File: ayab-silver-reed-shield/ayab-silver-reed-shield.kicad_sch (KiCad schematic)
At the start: 16 parts, among them J1 Power, J2 Digital/PWM, J3 Analog, J4 Digital/PWM, J5 DIN-7, J6 Barrel_Jack, K1 Relay_SPDT, Q1 2N2222A-TO92

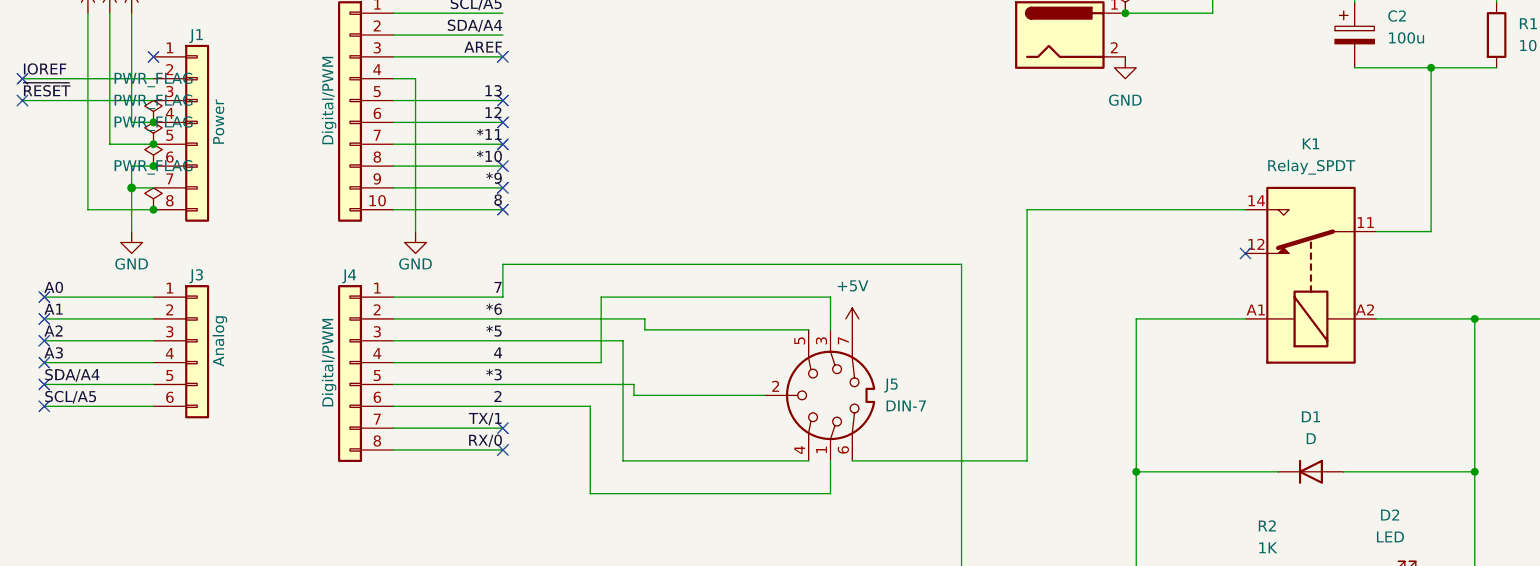
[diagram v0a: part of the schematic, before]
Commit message: Add footprints
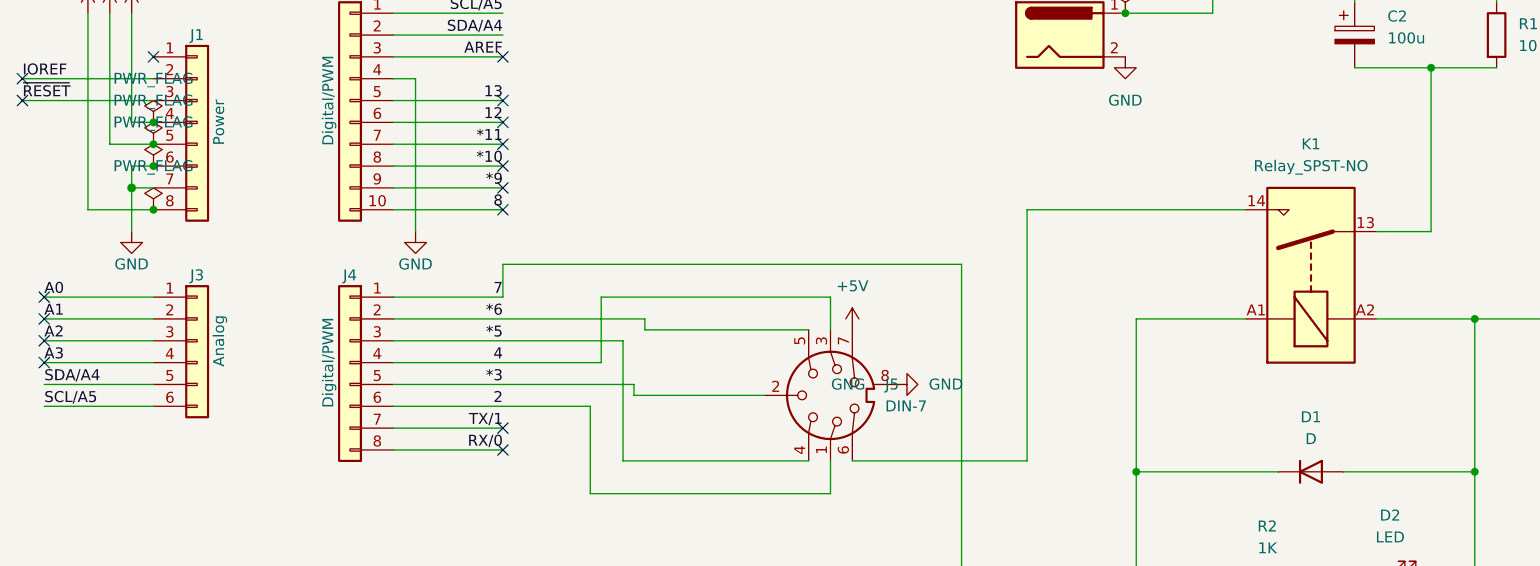
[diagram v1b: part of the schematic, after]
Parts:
- removed K1: Relay_SPDT, symbol Relay:Relay_SPDT
- added K1: Relay_SPST-NO, Locals:RELAY_G6DN-1A_OMR, symbol Relay:Relay_SPST-NO
- C2: footprint (none) -> Capacitor_THT:CP_Radial_D6.3mm_P2.50mm
- D1: footprint (none) -> Diode_THT:D_T-1_P5.08mm_Horizontal
- D2, D3: footprint (none) -> LED_THT:LED_D5.0mm
- J5: footprint (none) -> Connector_DIN:DIN-704-M10
- J6: footprint (none) -> Connector_BarrelJack:BarrelJack_Horizontal
- R1: footprint (none) -> Resistor_THT:R_Axial_Power_L20.0mm_W6.4mm_P25.40mm
- R2, R3: footprint (none) -> Resistor_THT:R_Axial_DIN0207_L6.3mm_D2.5mm_P7.62mm_Horizontal
- R4: footprint (none) -> Resistor_THT:R_Axial_DIN0207_L6.3mm_D2.5mm_P10.16mm_Horizontal
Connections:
- net +5V: now also K1.A1
- net GND: now also J5.8 (GNG)
- net at D1.2 (A), D2.1 (K), Q1.3 (C): now also K1.A2
- net at C2.2, R1.2: now also K1.13
- net at J5.6: now also K1.14
- no-connect marks 19 -> 16
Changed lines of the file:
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@@
 	)
 	(no_connect
-		(at 161.29 54.61)
-	)
-	(no_connect
 		(at 74.93 39.37)
 	)
@@
 	)
 	(no_connect
-		(at 21.59 69.85)
-	)
-	(no_connect
 		(at 21.59 64.77)
 	)
 	(no_connect
-		(at 21.59 72.39)
-	)
-	(no_connect
 		(at 21.59 59.69)
 	)
@@
 	)
 	(symbol
+		(lib_id "power:GND")
+		(at 120.65 69.85 90)
+		(unit 1)
+		(exclude_from_sim no)
+		(in_bom yes)
+		(on_board yes)
+		(dnp no)
+		(fields_autoplaced yes)
+		(property "Reference" "#PWR06"
+			(at 127 69.85 0)
+			(effects
+				(font
+					(size 1.27 1.27)
+				)
+				(hide yes)
+			)
+		)
+		(property "Value" "GND"
+			(at 124.46 69.8499 90)
+			(effects
+				(font
+					(size 1.27 1.27)
+				)
+				(justify right)
+			)
+		)
+		(property "Footprint" ""
+			(at 120.65 69.85 0)
+			(effects
+				(font
+					(size 1.27 1.27)
+				)
+				(hide yes)
+			)
+		)
+		(property "Datasheet" ""
+			(at 120.65 69.85 0)
+			(effects
+				(font
+					(size 1.27 1.27)
+				)
+				(hide yes)
+			)
+		)
+		(property "Description" "Power symbol creates a global label with name \"GND\" , ground"
+			(at 120.65 69.85 0)
+			(effects
+				(font
+					(size 1.27 1.27)
+				)
+				(hide yes)
+			)
+		)
+		(pin "1"
+		)
+		(instances
+			(project ""
+				(path "/e63e39d7-6ac0-4ffd-8aa3-1841a4541b55"
+					(reference "#PWR06")
+					(unit 1)
+				)
+			)
+		)
+	)
+	(symbol
 		(lib_id "Device:R")
 		(at 163.83 92.71 270)
@@
 			)
 		)
-		(property "Footprint" ""
+		(property "Footprint" "Resistor_THT:R_Axial_DIN0207_L6.3mm_D2.5mm_P7.62mm_Horizontal"
 			(at 163.83 90.932 90)
 			(effects
@@
 			)
 		)
-		(property "Footprint" ""
+		(property "Footprint" "Connector_BarrelJack:BarrelJack_Horizontal"
 			(at 140.97 30.226 0)
 			(effects
@@
 			)
 		)
-		(property "Footprint" ""
+		(property "Footprint" "Diode_THT:D_T-1_P5.08mm_Horizontal"
 			(at 168.91 80.01 0)
 			(effects
@@
 			)
 		)
-		(property "Footprint" ""
+		(property "Footprint" "Resistor_THT:R_Axial_DIN0207_L6.3mm_D2.5mm_P7.62mm_Horizontal"
 			(at 202.692 82.55 90)
 			(effects
@@
 			)
 		)
-		(property "Footprint" ""
+		(property "Footprint" "Resistor_THT:R_Axial_DIN0207_L6.3mm_D2.5mm_P10.16mm_Horizontal"
 			(at 163.83 101.092 90)
 			(effects
@@
 			)
 		)
-		(property "Footprint" ""
+		(property "Footprint" "LED_THT:LED_D5.0mm"
 			(at 176.53 102.87 0)
 			(effects
@@
 			)
 		)
-		(property "Footprint" ""
+		(property "Footprint" "Capacitor_THT:CP_Radial_D6.3mm_P2.50mm"
 			(at 174.9552 33.02 0)
 			(effects
@@
 			)
 		)
-		(property "Footprint" ""
+		(property "Footprint" "Resistor_THT:R_Axial_Power_L20.0mm_W6.4mm_P25.40mm"
 			(at 188.722 29.21 90)
 			(effects
@@
 			)
 		)
-		(property "Footprint" ""
+		(property "Footprint" "Connector_DIN:DIN-704-M10"
 			(at 113.03 71.12 0)
 			(effects
@@
 		(pin "2"
 		)
+		(pin "8"
+		)
 		(instances
 			(project ""
@@
 			)
 		)
-		(property "Footprint" ""
+		(property "Footprint" "LED_THT:LED_D5.0mm"
 			(at 176.53 92.71 0)
 			(effects
@@
 	)
 	(symbol
-		(lib_id "PCM_Transistor_BJT_AKL:2N2222A-TO92")
-		(at 204.47 64.77 90)
+		(lib_id "Relay:Relay_SPST-NO")
+		(at 168.91 57.15 90)
 		(unit 1)
 		(exclude_from_sim no)
@@
 		(dnp no)
 		(fields_autoplaced yes)
-		(property "Reference" "Q1"
-			(at 204.47 55.88 90)
+		(property "Reference" "K1"
+			(at 168.91 41.91 90)
 			(effects
 				(font
@@
 			)
 		)
-		(property "Value" "2N2222A-TO92"
-			(at 204.47 58.42 90)
+		(property "Value" "Relay_SPST-NO"
+			(at 168.91 44.45 90)
 			(effects
 				(font
@@
 			)
 		)
-		(property "Footprint" "PCM_Package_TO_SOT_THT_AKL:TO-92_Inline_Wide_EBC"
-			(at 201.93 59.69 0)
+		(property "Footprint" "Locals:RELAY_G6DN-1A_OMR"
+			(at 170.18 45.72 0)
 			(effects
 				(font
 					(size 1.27 1.27)
 				)
+				(justify left)
 				(hide yes)
 			)
 		)
-		(property "Datasheet" "https://www.tme.eu/Document/f56ae9fa05736feb390d26bab71fb0d5/2n2222a.pdf"
-			(at 204.47 64.77 0)
+		(property "Datasheet" "~"
+			(at 168.91 57.15 0)
 			(effects
 				(font
@@
 			)
 		)
-		(property "Description" "NPN TO-92 transistor, 40V, 0.6A, 625mW, Alternate KiCAD Library"
-			(at 204.47 64.77 0)
+		(property "Description" "Relay SPST, normally open, EN50005"
+			(at 168.91 57.15 0)
 			(effects
 				(font
@@
 			)
 		)
-		(pin "2"
+		(property "Ref" "OMRON G6DN-1A-SL DC5"
+			(at 168.91 57.15 90)
+			(effects
+				(font
+					(size 1.27 1.27)
+				)
+				(hide yes)
+			)
 		)
-		(pin "3"
+		(property "Manufacturer" "OMRON"
+			(at 168.91 57.15 90)
+			(effects
+				(font
+					(size 1.27 1.27)
+				)
+				(hide yes)
+			)
 		)
-		(pin "1"
+		(property "LCSC" "https://www.lcsc.com/product-detail/C397208.html?s_z=n_C397208"
+			(at 168.91 57.15 90)
+			(effects
+				(font
+					(size 1.27 1.27)
+				)
+				(hide yes)
+			)
+		)
+		(pin "14"
+		)
+		(pin "13"
+		)
+		(pin "A1"
+		)
+		(pin "A2"
 		)
 		(instances
 			(project ""
 				(path "/e63e39d7-6ac0-4ffd-8aa3-1841a4541b55"
-					(reference "Q1")
+					(reference "K1")
 					(unit 1)
 				)
@@
 	)
 	(symbol
-		(lib_id "Relay:Relay_SPDT")
-		(at 168.91 57.15 90)
+		(lib_id "PCM_Transistor_BJT_AKL:2N2222A-TO92")
+		(at 204.47 64.77 90)
 		(unit 1)
 		(exclude_from_sim no)
@@
 		(dnp no)
 		(fields_autoplaced yes)
-		(property "Reference" "K1"
-			(at 168.91 41.91 90)
+		(property "Reference" "Q1"
+			(at 204.47 55.88 90)
 			(effects
 				(font
@@
 			)
 		)
-		(property "Value" "Relay_SPDT"
-			(at 168.91 44.45 90)
+		(property "Value" "2N2222A-TO92"
+			(at 204.47 58.42 90)
 			(effects
 				(font
@@
 			)
 		)
-		(property "Footprint" ""
-			(at 170.18 45.72 0)
+		(property "Footprint" "PCM_Package_TO_SOT_THT_AKL:TO-92_Inline_Wide_EBC"
+			(at 201.93 59.69 0)
 			(effects
 				(font
 					(size 1.27 1.27)
 				)
-				(justify left)
 				(hide yes)
 			)
 		)
-		(property "Datasheet" "~"
-			(at 168.91 57.15 0)
+		(property "Datasheet" "https://www.tme.eu/Document/f56ae9fa05736feb390d26bab71fb0d5/2n2222a.pdf"
+			(at 204.47 64.77 0)
 			(effects
 				(font
@@
 			)
 		)
-		(property "Description" "Relay SPDT, monostable, EN50005"
-			(at 168.91 57.15 0)
+		(property "Description" "NPN TO-92 transistor, 40V, 0.6A, 625mW, Alternate KiCAD Library"
+			(at 204.47 64.77 0)
 			(effects
 				(font
@@
 			)
 		)
-		(pin "A1"
-		)
-		(pin "A2"
-		)
-		(pin "12"
+		(pin "2"
 		)
-		(pin "11"
+		(pin "3"
 		)
-		(pin "14"
+		(pin "1"
 		)
 		(instances
 			(project ""
 				(path "/e63e39d7-6ac0-4ffd-8aa3-1841a4541b55"
-					(reference "K1")
+					(reference "Q1")
 					(unit 1)
 				)

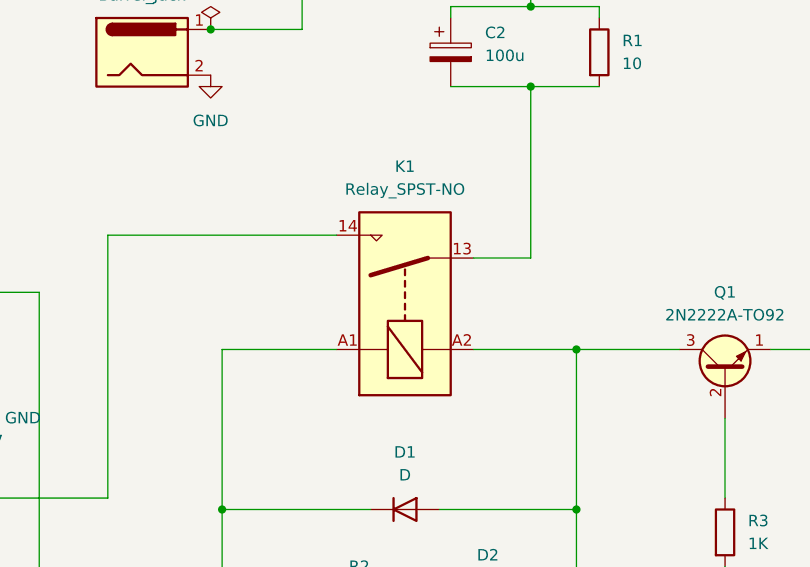
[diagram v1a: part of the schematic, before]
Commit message: Add footprints
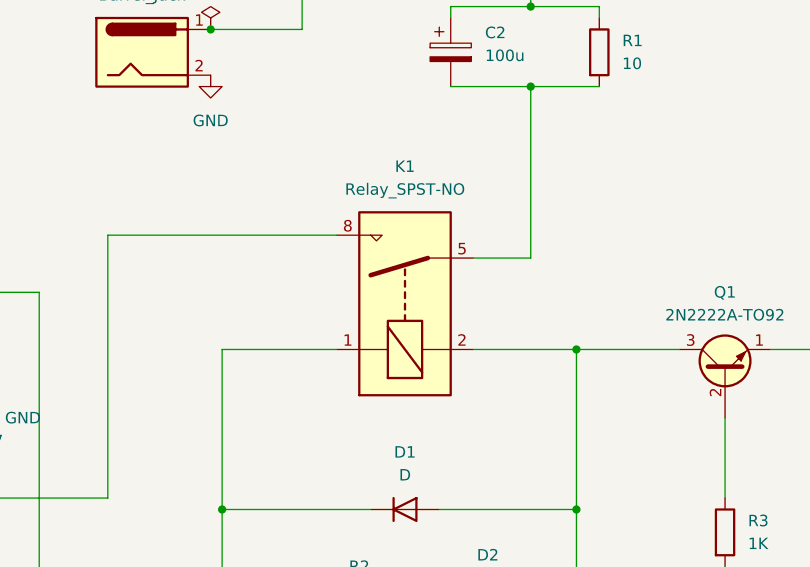
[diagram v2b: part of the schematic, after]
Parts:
- J5: footprint Connector_DIN:DIN-704-M10 -> Locals:DIN-704-M10
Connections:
- net +5V: now also K1.1; no longer K1.A1
- net at D1.2 (A), D2.1 (K), Q1.3 (C): now also K1.2; no longer K1.A2
- net at C2.2, R1.2: now also K1.5; no longer K1.13
- net at J5.6: now also K1.8; no longer K1.14
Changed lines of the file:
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@@
 			)
 		)
-		(property "Footprint" "Connector_DIN:DIN-704-M10"
+		(property "Footprint" "Locals:DIN-704-M10"
 			(at 113.03 71.12 0)
 			(effects
@@
 			)
 		)
-		(pin "14"
-		)
-		(pin "13"
-		)
-		(pin "A1"
-		)
-		(pin "A2"
-		)
-		(instances
+		(pin "1"
+		)
+		(pin "5"
+		)
+		(pin "8"
+		)
+		(pin "2"
+		)
+		(instances

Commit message: Add PCB board design
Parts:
- J1, J4: footprint Connector_PinSocket_2.54mm:PinSocket_1x08_P2.54mm_Vertical -> Connector_PinHeader_2.54mm:PinHeader_1x08_P2.54mm_Vertical
- J2: footprint Connector_PinSocket_2.54mm:PinSocket_1x10_P2.54mm_Vertical -> Connector_PinHeader_2.54mm:PinHeader_1x10_P2.54mm_Vertical
- J3: footprint Connector_PinSocket_2.54mm:PinSocket_1x06_P2.54mm_Vertical -> Connector_PinHeader_2.54mm:PinHeader_1x06_P2.54mm_Vertical
- R2, R3: footprint Resistor_THT:R_Axial_DIN0207_L6.3mm_D2.5mm_P7.62mm_Horizontal -> Resistor_THT:R_Axial_DIN0207_L6.3mm_D2.5mm_P2.54mm_Vertical
- R4: footprint Resistor_THT:R_Axial_DIN0207_L6.3mm_D2.5mm_P10.16mm_Horizontal -> Resistor_THT:R_Axial_DIN0207_L6.3mm_D2.5mm_P2.54mm_Vertical
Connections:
- net SCL/A5: no longer J2.1 (Pin_1)
- net SDA/A4: no longer J2.2 (Pin_2)
- new net A4: J2.2 (Pin_2)
- new net A5: J2.1 (Pin_1)
- no-connect marks 16 -> 20
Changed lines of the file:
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@@
+	)
+	(no_connect
+		(at 21.59 69.85)
 	)
 	(no_connect
@@
 	)
 	(no_connect
+		(at 21.59 72.39)
+	)
+	(no_connect
 		(at 74.93 49.53)
 	)
@@
 	)
 	(no_connect
+		(at 74.93 26.67)
+	)
+	(no_connect
 		(at 74.93 74.93)
 	)
@@
 	)
 	(no_connect
+		(at 74.93 29.21)
+	)
+	(no_connect
 		(at 21.59 64.77)
 	)
@@
 		)
 	)
-	(label "SDA{slash}A4"
+	(label "A4"
 		(at 74.93 29.21 180)
 		(effects
@@
 		)
 	)
-	(label "SCL{slash}A5"
+	(label "A5"
 		(at 74.93 26.67 180)
 		(effects
@@
 			)
 		)
-		(property "Footprint" "Connector_PinSocket_2.54mm:PinSocket_1x08_P2.54mm_Vertical"
+		(property "Footprint" "Connector_PinHeader_2.54mm:PinHeader_1x08_P2.54mm_Vertical"
 			(at 39.37 39.37 0)
 			(effects
@@
 			)
 		)
-		(property "Footprint" "Connector_PinSocket_2.54mm:PinSocket_1x10_P2.54mm_Vertical"
+		(property "Footprint" "Connector_PinHeader_2.54mm:PinHeader_1x10_P2.54mm_Vertical"
 			(at 57.15 36.83 0)
 			(effects
@@
 			)
 		)
-		(property "Footprint" "Connector_PinSocket_2.54mm:PinSocket_1x06_P2.54mm_Vertical"
+		(property "Footprint" "Connector_PinHeader_2.54mm:PinHeader_1x06_P2.54mm_Vertical"
 			(at 39.37 64.77 0)
 			(effects
@@
 			)
 		)
-		(property "Footprint" "Connector_PinSocket_2.54mm:PinSocket_1x08_P2.54mm_Vertical"
+		(property "Footprint" "Connector_PinHeader_2.54mm:PinHeader_1x08_P2.54mm_Vertical"
 			(at 57.15 67.31 0)
 			(effects
@@
 			)
 		)
-		(property "Footprint" "Resistor_THT:R_Axial_DIN0207_L6.3mm_D2.5mm_P7.62mm_Horizontal"
+		(property "Footprint" "Resistor_THT:R_Axial_DIN0207_L6.3mm_D2.5mm_P2.54mm_Vertical"
 			(at 163.83 90.932 90)
 			(effects
@@
 			)
 		)
-		(property "Footprint" "Resistor_THT:R_Axial_DIN0207_L6.3mm_D2.5mm_P7.62mm_Horizontal"
+		(property "Footprint" "Resistor_THT:R_Axial_DIN0207_L6.3mm_D2.5mm_P2.54mm_Vertical"
 			(at 202.692 82.55 90)
 			(effects
@@
 			)
 		)
-		(property "Footprint" "Resistor_THT:R_Axial_DIN0207_L6.3mm_D2.5mm_P10.16mm_Horizontal"
+		(property "Footprint" "Resistor_THT:R_Axial_DIN0207_L6.3mm_D2.5mm_P2.54mm_Vertical"
 			(at 163.83 101.092 90)
 			(effects

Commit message: fix: remove dead reference
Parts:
- C2: footprint Capacitor_THT:CP_Radial_D6.3mm_P2.50mm -> Locals:CP_6.3x11mm_horiz-R
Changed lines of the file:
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@@
 			)
 		)
-		(property "Footprint" "Capacitor_THT:CP_Radial_D6.3mm_P2.50mm"
+		(property "Footprint" "Locals:CP_6.3x11mm_horiz-R"
 			(at 174.9552 33.02 0)
 			(effects

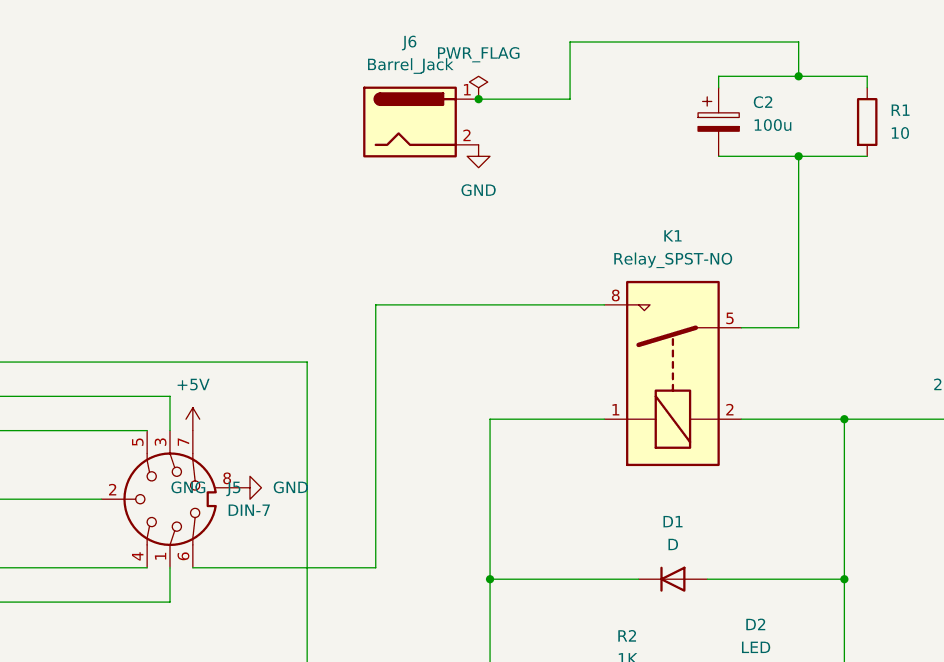
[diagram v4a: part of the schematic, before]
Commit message: fix: invert din pins
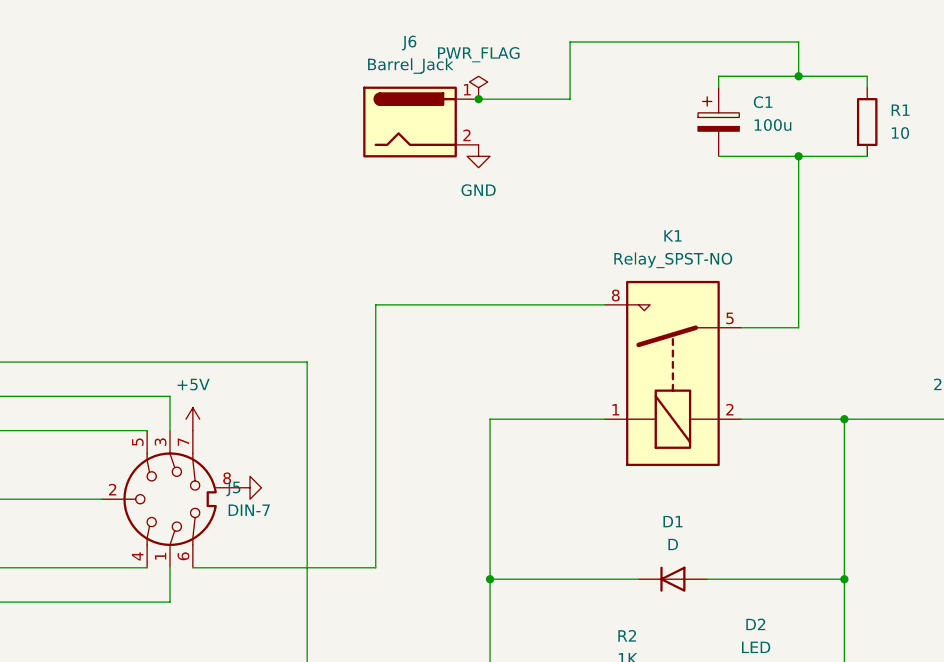
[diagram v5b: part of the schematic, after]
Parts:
- D1: footprint Diode_THT:D_T-1_P5.08mm_Horizontal -> Diode_THT:D_DO-41_SOD81_P7.62mm_Horizontal
- Q1: footprint PCM_Package_TO_SOT_THT_AKL:TO-92_Inline_Wide_EBC -> Package_TO_SOT_THT:TO-92_Inline
- renumbered C2 to C1
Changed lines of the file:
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@@
 				)
 				(justify right)
+				(hide yes)
 			)
 		)
@@
 			)
 		)
-		(property "Footprint" "Diode_THT:D_T-1_P5.08mm_Horizontal"
+		(property "Footprint" "Diode_THT:D_DO-41_SOD81_P7.62mm_Horizontal"
 			(at 168.91 80.01 0)
 			(effects
@@
 		(dnp no)
 		(fields_autoplaced yes)
-		(property "Reference" "C2"
+		(property "Reference" "C1"
 			(at 177.8 27.0509 0)
 			(effects
@@
 			(project ""
 				(path "/e63e39d7-6ac0-4ffd-8aa3-1841a4541b55"
-					(reference "C2")
+					(reference "C1")
 					(unit 1)
 				)
@@
 			)
 		)
-		(property "Footprint" "PCM_Package_TO_SOT_THT_AKL:TO-92_Inline_Wide_EBC"
+		(property "Footprint" "Package_TO_SOT_THT:TO-92_Inline"
 			(at 201.93 59.69 0)
 			(effects
